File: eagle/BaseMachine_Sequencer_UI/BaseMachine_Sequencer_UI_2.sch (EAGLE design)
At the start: 4 parts, among them SW1 AK_TCTSW, SW2 AK_TCTSW

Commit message: Update: UI & UI2 Board Design
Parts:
- added JP2: PWR1, pinhead:PINHD-1X2/90
- added JP3: PWR2, pinhead:PINHD-1X2
- added JP4: PWR3, pinhead:PINHD-1X2
- added JP5: PWR4, pinhead:PINHD-1X2
- added JP6: PWR5, pinhead:PINHD-1X2
- added SW3: AK_TCTSW, mylib2:AK_TCTSW
- JP1: value (none) -> SW1
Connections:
- removed net N$3: JP1.1, RE1.A
- removed net N$6: JP1.4, SW2.S, SW2.S@1
- new net N$1: JP1.2, RE1.A
- new net N$2: JP1.5, SW2.S, SW2.S@1
- new net N$7: JP1.1, SW3.S, SW3.S@1
- new net VCC: JP2.1, JP3.1, JP4.1, JP5.1, JP6.1
- net GND: now also JP2.2, JP3.2, JP4.2, JP5.2, JP6.2, SW3.P, SW3.P@1; no longer JP1.5
- net N$4: now also JP1.3; no longer JP1.2
- net N$5: now also JP1.4; no longer JP1.3
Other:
- moved on the sheet: JP1, RE1, SW1, SW2

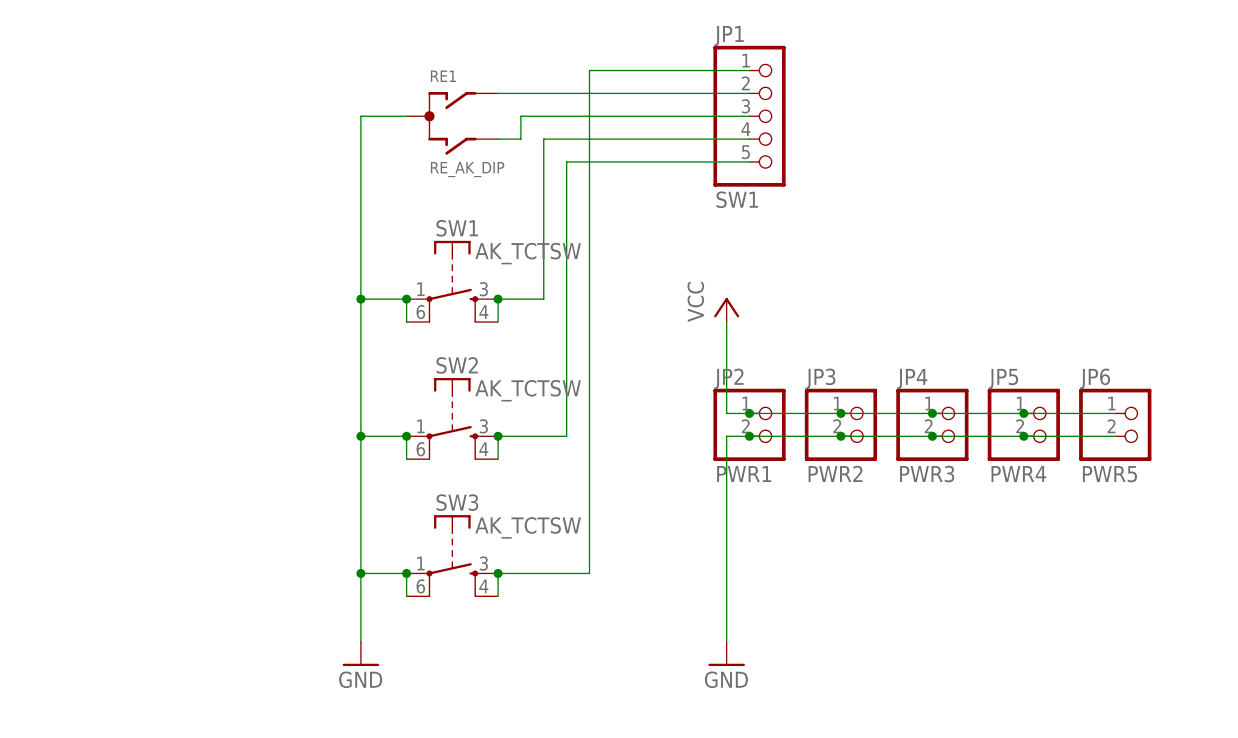
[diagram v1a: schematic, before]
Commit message: Add: Nucleo firmware's binaries
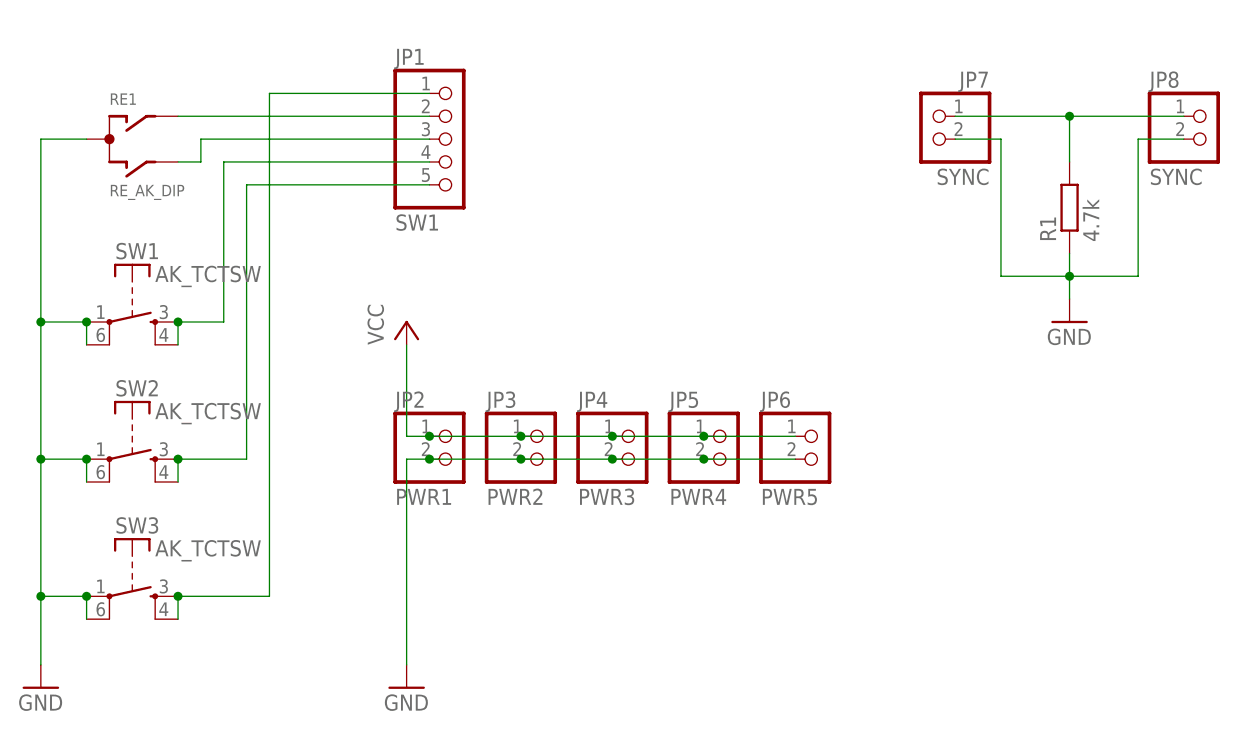
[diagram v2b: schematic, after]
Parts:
- added JP7: SYNC, pinhead:PINHD-1X2/90
- added JP8: SYNC, pinhead:PINHD-1X2
- added R1: 4.7k, rcl:R-EU_0207/7
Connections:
- new net N$6: JP7.1, JP8.1, R1.2
- net GND: now also JP7.2, JP8.2, R1.1
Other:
- moved on the sheet: JP1, JP2, JP3, JP4, JP5, JP6, RE1, SW1, SW2, SW3
